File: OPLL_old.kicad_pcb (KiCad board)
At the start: 4 copper layers, 50 parts, among them J1 Conn_Coaxial, J2 Conn_Coaxial, J3 B4B-PH-K-S_LF__SN_, J4 Conn_Coaxial, J5 Conn_Coaxial, J6 Conn_Coaxial, J7 OSTTC042162, U1 ADF4107, U2 Opamp_Quad, U3 OPA847xDBV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

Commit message: First OPLL iteration
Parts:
- added C12: C_Polarized_Small_US, Capacitor_THT:CP_Radial_D10.0mm_P5.00mm, F.Cu at (136.7, 147.3)
- added C13: C_Polarized_Small_US, Capacitor_THT:CP_Radial_D10.0mm_P5.00mm, F.Cu at (50.0, 147.5)
- added D2: SA15CA-TP, Diode_THT:D_DO-201AE_P15.24mm_Horizontal, F.Cu at (80.9, 147.5)
- added D3: SA15CA-TP, Diode_THT:D_DO-201AE_P15.24mm_Horizontal, F.Cu at (109.7, 147.4)
- added F1: Polyfuse RXEF040, Fuse:Fuse_BelFuse_0ZRE0005FF_L8.3mm_W3.8mm, F.Cu at (87.9, 145.8)
- added F2: Polyfuse RXEF040, Fuse:Fuse_BelFuse_0ZRE0005FF_L8.3mm_W3.8mm, F.Cu at (103.2, 147.4)
- added H1: MountingHole, MountingHole:MountingHole_3.2mm_M3, F.Cu at (132.0, 110.6)
- added H2: MountingHole, MountingHole:MountingHole_3.2mm_M3, F.Cu at (70.3, 110.5)
- moved D1 126.4 mm to (117.7, 119.2), turned to -90 degrees
- moved R3 118.4 mm to (63.3, 117.2), turned to 90 degrees
- moved J6 110.4 mm to (141.7, 134.9), turned to 180 degrees
- moved J4 109.1 mm to (141.7, 122.2), turned to 180 degrees
- moved J5 100.3 mm to (141.7, 109.6), turned to 180 degrees
- moved C5 95.5 mm to (63.3, 114.8), turned to -90 degrees
- moved C6 94.0 mm to (98.7, 114.6), turned to 180 degrees
- moved R5 88.6 mm to (135.4, 122.2), turned to 180 degrees
- moved R20 79.6 mm to (97.6, 118.8), turned to -90 degrees
- moved R17 75.4 mm to (99.9, 120.6)
- moved R15 73.6 mm to (127.8, 120.2), turned to -90 degrees
- moved C7 73.1 mm to (124.9, 120.7)
- moved R10 72.9 mm to (98.8, 113.2), turned to 180 degrees
- moved R22 72.6 mm to (135.4, 134.9), turned to 180 degrees
- moved R11 70.7 mm to (102.0, 115.1), turned to -90 degrees
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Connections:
- J7 pad 3: +15V -> Net-(J7-Pad3)
- J7 pad 4: -15V -> Net-(J7-Pad4)
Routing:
- net Net-(R20-Pad1): track 0.00 -> 49.3 mm, vias 0 -> 2
- net Net-(R5-Pad2): track 11.0 -> 59.8 mm, vias 0 -> 2
- net GND2: track 0.00 -> 48.5 mm, vias 0 -> 26
- net +15V: track 0.00 -> 44.4 mm, vias 0 -> 2
- net Net-(C8-Pad1): track 0.00 -> 40.0 mm, vias 0 -> 2
- net Net-(C8-Pad2): track 0.00 -> 37.7 mm, vias 0 -> 2
- net Net-(C7-Pad1): track 0.00 -> 30.0 mm
- net Net-(R17-Pad2): track 0.00 -> 29.0 mm, vias 0 -> 2
- net -15V: track 0.00 -> 28.6 mm, vias 0 -> 3
- net Net-(J5-Pad1): track 0.00 -> 24.3 mm
- net Net-(R3-Pad1): track 15.6 -> 30.0 mm
- net +5VD: track 24.6 -> 38.4 mm, vias 2 -> 0
- net -5VA: track 53.5 -> 65.5 mm
- net Net-(J3-Pad4): track 20.2 -> 32.1 mm, vias 0 -> 2
- net Net-(J4-Pad1): track 17.1 -> 5.74 mm
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- added copper zone on B.Cu, net +15V
- added copper zone on B.Cu, net -15V
- added copper zone on F.Cu, net GND1
- added copper zone on In1.Cu, net GND1
- added copper zone on F.Cu, net GND2
- added copper zone on In2.Cu, net GND2
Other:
- board outline added: 103.9 x 51 mm
- board text added: "Data CLK LE CE"
- board text added: "Error Out"
- board text added: "FET Out"
- board text added: "Integrator Latch"
- board text added: "Piezo Out"
- board text added: "Power In"
- board text added: "REF In"
- board text added: "RFIN"

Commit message: it2
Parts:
- added C14: 10p, Capacitor_SMD:C_0402_1005Metric, F.Cu at (72.6, 45.2)
- added C15: 0.1u, Capacitor_SMD:C_0402_1005Metric, F.Cu at (72.6, 47.8)
- added C16: 10p, Capacitor_SMD:C_0402_1005Metric, F.Cu at (72.6, 46.5)
- added C17: T58W9105M035C0500, Capacitor_SMD:C_0805_2012Metric_Pad1.18x1.45mm_HandSolder, F.Cu at (81.3, 73.8)
- added C18: T58W9105M035C0500, Capacitor_SMD:C_0805_2012Metric_Pad1.18x1.45mm_HandSolder, F.Cu at (81.3, 68.7)
- added C19: T58W9105M035C0500, Capacitor_SMD:C_0805_2012Metric_Pad1.18x1.45mm_HandSolder, F.Cu at (72.8, 62.4)
- added C20: T58W9105M035C0500, Capacitor_SMD:C_0805_2012Metric_Pad1.18x1.45mm_HandSolder, F.Cu at (70.8, 53.7)
- added C21: T58W9105M035C0500, Capacitor_SMD:C_0805_2012Metric_Pad1.18x1.45mm_HandSolder, F.Cu at (112.9, 59.5)
- added C22: T58W9105M035C0500, Capacitor_SMD:C_0805_2012Metric_Pad1.18x1.45mm_HandSolder, F.Cu at (81.2, 89.2)
- added C23: T58W9105M035C0500, Capacitor_SMD:C_0805_2012Metric_Pad1.18x1.45mm_HandSolder, F.Cu at (118.2, 59.5)
- added C24: T58W9105M035C0500, Capacitor_SMD:C_0805_2012Metric_Pad1.18x1.45mm_HandSolder, F.Cu at (81.2, 84.2)
- added C25: T58W9105M035C0500, Capacitor_SMD:C_0805_2012Metric_Pad1.18x1.45mm_HandSolder, F.Cu at (77.1, 48.5)
- added C26: T58W9105M035C0500, Capacitor_SMD:C_0805_2012Metric_Pad1.18x1.45mm_HandSolder, F.Cu at (94.1, 47.5)
- C10, C11: value 100p -> 0.1u
- C9: value 100p -> 10p
- J3: value B4B-PH-K-S_LF__SN_ -> OSTTC050162; footprint digikey-footprints:PinHeader_1x4_P2mm_Drill1mm -> digikey-footprints:Term_Block_1x5_P5mm
- moved J4 106.6 mm to (53.8, 61.9), turned to 0 degrees
- moved J6 106.5 mm to (53.8, 74.8), turned to 0 degrees
- moved R22 101.6 mm to (93.1, 42.5)
- moved R5 96.9 mm to (81.2, 41.9)
- moved J5 90.6 mm to (53.8, 87.7), turned to 0 degrees
- moved H2 89.1 mm to (118.0, 35.3)
- moved U5 86.6 mm to (115.5, 47.9), turned to 90 degrees
- moved C11 85.2 mm to (72.6, 43.8), turned to 0 degrees
- moved C13 84.7 mm to (91.5, 73.6), turned to 90 degrees
- moved D2 82.9 mm to (103.2, 67.7), turned to 90 degrees
- moved J7 81.4 mm to (118.2, 65.3), turned to -90 degrees
- moved U7 79.3 mm to (65.6, 59.1)
- moved C9 77.6 mm to (63.9, 51.7), turned to 0 degrees
- moved D3 76.1 mm to (103.2, 71.6), turned to -90 degrees
- moved R1 76.0 mm to (61.3, 38.2), turned to -90 degrees
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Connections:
- C10 pad 1: GND1 -> +3V3
- C10 pad 2: +3V3 -> GND
- C11 pad 1: GND1 -> +5VD
- C11 pad 2: +5VD -> GND
- C12 pad 1: -15V -> GND
- C12 pad 2: GND2 -> -15V
- C13 pad 1: GND2 -> +15V
- C13 pad 2: +15V -> GND
- C4 pad 2: GND1 -> GND
- C5 pad 1: GND2 -> GND
- C6 pad 1: GND2 -> GND
- C9 pad 2: GND1 -> GND
- D1 pad 2: GND2 -> GND
- D2 pad 2: GND2 -> GND
- D3 pad 1: -15V -> GND
- D3 pad 2: GND2 -> -15V
- F1 pad 2: Net-(J7-Pad3) -> Net-(F1-Pad2)
- J1 pad 2: GND1 -> GND
- J2 pad 2: GND1 -> GND
- J3 pad 1: Net-(J3-Pad1) -> GND
- J3 pad 2: Net-(J3-Pad2) -> Net-(U1-Pad10)
- J4 pad 2: GND2 -> GND
- J5 pad 2: GND2 -> GND
- J6 pad 2: GND2 -> GND
- J7 pad 1: GND2 -> GND
- J7 pad 2: GND1 -> Net-(F1-Pad2)
- J7 pad 3: Net-(J7-Pad3) -> GND
- R1 pad 2: GND1 -> GND
- R10 pad 1: GND2 -> GND
- R15 pad 1: GND2 -> GND
- R19 pad 2: GND2 -> GND
- R2 pad 2: GND1 -> GND
- R21 pad 2: GND2 -> GND
- R4 pad 2: GND2 -> GND
- R7 pad 2: GND2 -> GND
- RV1 pad 3: GND2 -> GND
- U1 pad 10: Net-(J3-Pad1) -> Net-(U1-Pad10)
- U1 pad 13: Net-(J3-Pad2) -> Net-(U1-Pad13)
- U1 pad 3: GND2 -> GND
- U1 pad 4: GND1 -> GND
- U1 pad 9: GND1 -> GND
- U2 pad 11: GND2 -> GND
- U2 pad 5: GND2 -> GND
- U4 pad 2: GND1 -> GND
- U5 pad 2: GND2 -> GND
- U6 pad 2: GND2 -> GND
- U7 pad 2: GND1 -> GND
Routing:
- net Net-(J5-Pad1): track 24.3 -> 74.4 mm, vias 0 -> 1
- net GND2: track 48.5 -> 0.00 mm, vias 26 -> 0
- net Net-(J6-Pad1): track 5.79 -> 54.1 mm, vias 0 -> 1
- net Net-(R20-Pad1): track 49.3 -> 4.09 mm, vias 2 -> 0
- net Net-(R5-Pad2): track 59.8 -> 17.2 mm, vias 2 -> 0
- net Net-(J3-Pad1): track 37.1 -> 0.00 mm, vias 2 -> 0
- net +15V: track 44.4 -> 8.91 mm
- net -5VA: track 65.5 -> 30.9 mm, vias 0 -> 3
- net Net-(J3-Pad2): track 34.5 -> 0.00 mm, vias 2 -> 0
- net Net-(J4-Pad1): track 5.74 -> 39.7 mm, vias 0 -> 1
- net GND: track 0.00 -> 30.2 mm, vias 0 -> 31
- net Net-(U1-Pad13): track 0.00 -> 29.5 mm
- net Net-(R17-Pad2): track 29.0 -> 2.23 mm, vias 2 -> 0
- net +5VA: track 42.6 -> 17.0 mm, vias 0 -> 2
- net -15V: track 28.6 -> 4.07 mm, vias 3 -> 1
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- added copper zone on In2.Cu, net +3V3
- added copper zone on In2.Cu, net +5VA
- added copper zone on B.Cu, net +5VD
- added copper zone on B.Cu, net -5VA
- added copper zone on In2.Cu, net -5VA
- added copper zone on F.Cu, net GND
- added copper zone on In1.Cu, net GND
- added copper zone on In2.Cu, net GND
- removed copper zone on F.Cu, net GND1
- removed copper zone on In1.Cu, net GND1
- removed copper zone on F.Cu, net GND2
- removed copper zone on In2.Cu, net GND2
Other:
- board size 103.9 x 51 mm -> 77.1 x 64.2 mm
- board text added: "GND +15V GND -15V"
- board text added: "GND CE CLK DATA LE"
- board text added: "REF IN"
- board text removed: "Data CLK LE CE"
- board text removed: "Power In"
- board text removed: "REF In"
- board text removed: "RFIN"

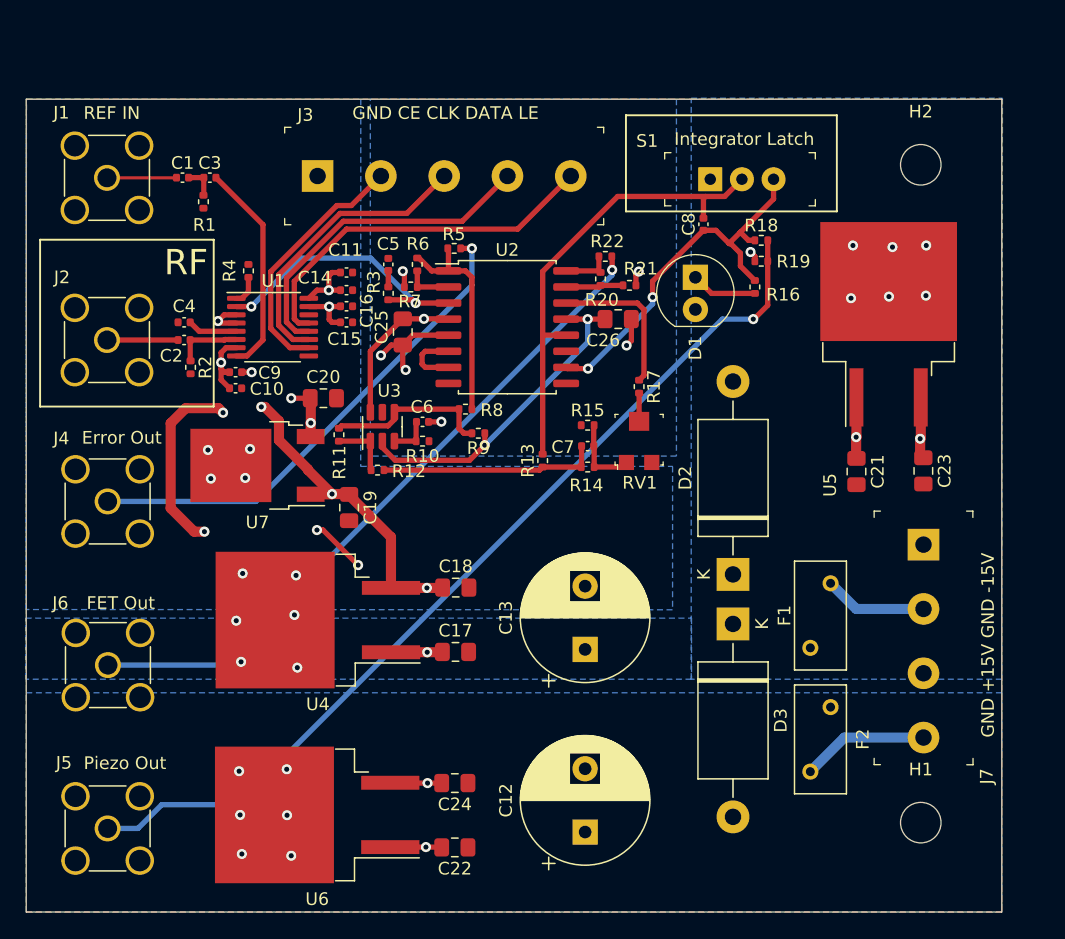
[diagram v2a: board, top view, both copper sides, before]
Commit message: FET update
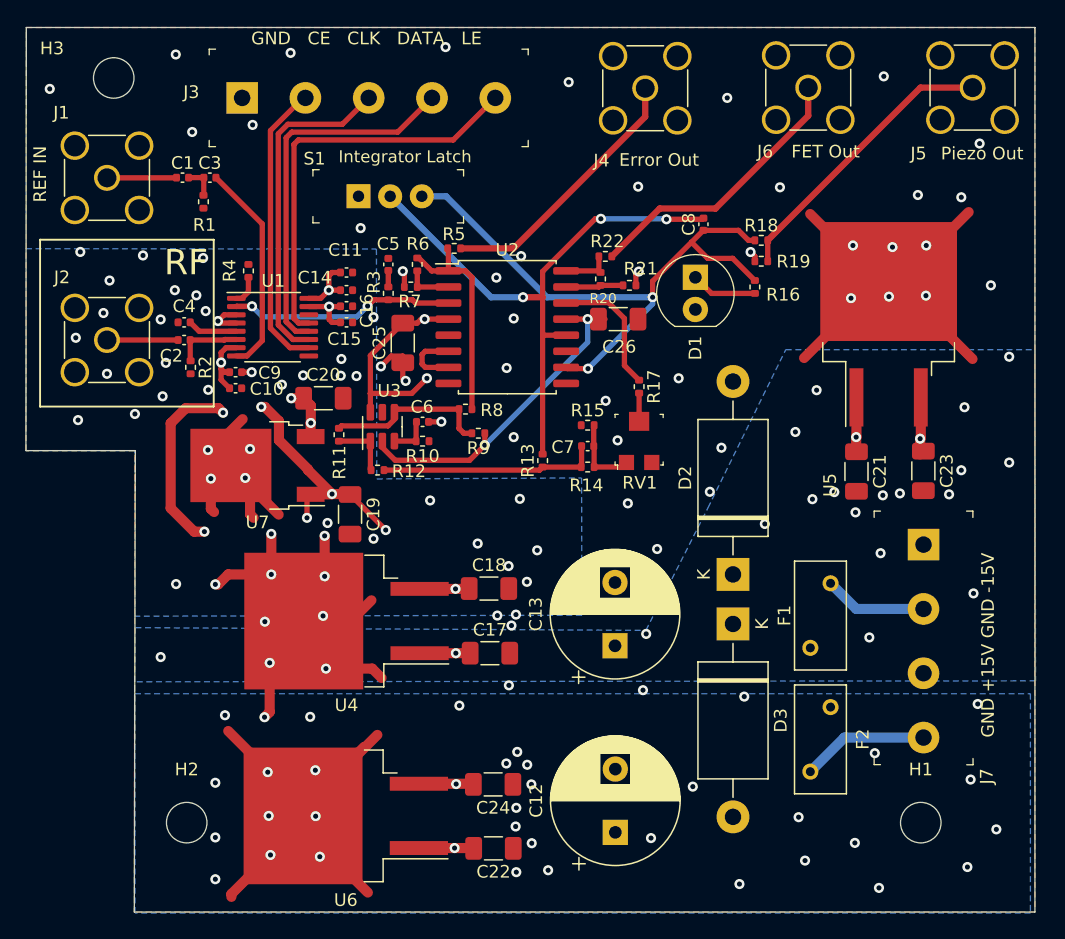
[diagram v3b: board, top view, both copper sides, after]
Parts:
- added H3: MountingHole, MountingHole:MountingHole_3.2mm_M3, F.Cu at (54.3, 28.4)
- C17, C18, C19, C20, C21, C22, C23, C24, C25, C26: footprint Capacitor_SMD:C_0805_2012Metric_Pad1.18x1.45mm_HandSolder -> Capacitor_SMD:C_1206_3216Metric_Pad1.33x1.80mm_HandSolder
- moved J5 90.0 mm to (122.1, 29.2)
- moved H2 77.9 mm to (60.0, 87.3)
- moved J6 71.7 mm to (109.1, 29.2)
- moved J4 53.6 mm to (96.2, 29.3)
- moved S1 27.8 mm to (73.6, 37.8)
- moved J3 8.58 mm to (64.4, 30.0)
- moved C22 3.05 mm to (84.3, 89.3)
- moved C24 3.03 mm to (84.2, 84.3)
- moved C17 2.72 mm to (84.0, 73.9)
- moved C18 2.62 mm to (83.9, 68.8)
- moved C12 2.39 mm to (93.9, 88.0)
- moved C13 2.38 mm to (93.9, 73.3)
- moved U4 2.26 mm to (72.6, 71.3)
- moved U6 2.26 mm to (72.6, 86.7)
- moved C25 0.87 mm to (77.1, 49.4)
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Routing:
- net GND: track 30.2 -> 109.4 mm, vias 31 -> 144
- net Net-(J5-Pad1): track 74.4 -> 22.8 mm, vias 1 -> 0
- net Net-(J6-Pad1): track 54.1 -> 22.3 mm, vias 1 -> 0
- net Net-(J4-Pad1): track 39.7 -> 21.1 mm, vias 1 -> 0
- net Net-(C8-Pad1): track 30.7 -> 48.7 mm
- net Net-(C8-Pad2): track 36.8 -> 46.1 mm, vias 0 -> 3
- net +5VD: track 49.5 -> 42.3 mm
- net +5VA: track 17.0 -> 21.3 mm, vias 2 -> 3
- net Net-(R3-Pad1): track 22.1 -> 17.8 mm
- net Net-(J3-Pad2): track 20.0 -> 23.1 mm
- net Net-(J3-Pad3): track 23.1 -> 26.3 mm
- net Net-(J3-Pad4): track 26.3 -> 29.5 mm
- net Net-(J3-Pad5): track 29.5 -> 32.5 mm
- net Net-(R17-Pad1): track 12.1 -> 10.5 mm
- net +15V: track 8.91 -> 8.35 mm
- removed copper zone on B.Cu, net -5VA
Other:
- board size 77.1 x 64.2 mm -> 79.7 x 69.9 mm
